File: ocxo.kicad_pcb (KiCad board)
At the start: 2 copper layers, 50 x 50 mm, 21 parts, among them J1 Conn_01x02, J2 Conn_01x01, J3 Conn_Coaxial, J4 Conn_01x01, J5 Conn_01x01, J6 Conn_01x01, J7 Conn_Coaxial, Q1 ENE3311 OCXO, U1 KA78M05_TO252, U2 LM4140

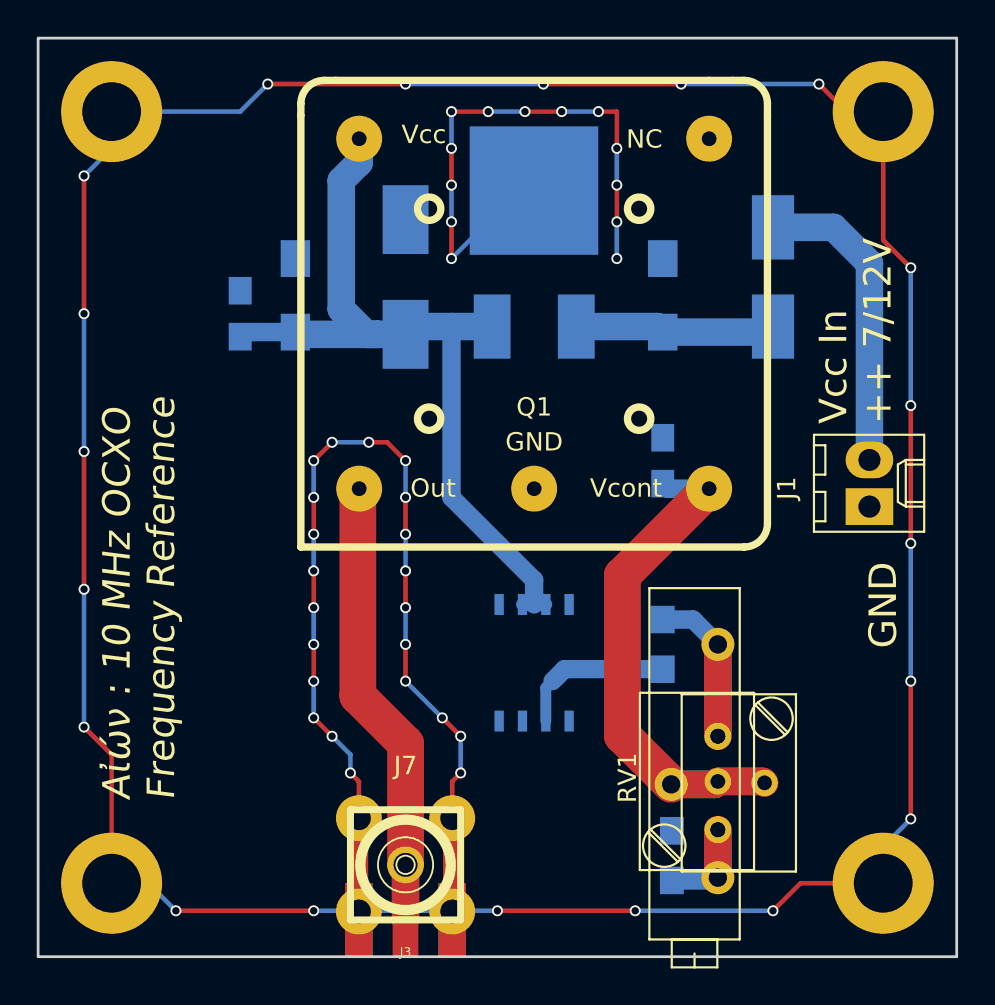
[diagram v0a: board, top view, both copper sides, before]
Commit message: via stitching added, new gerber
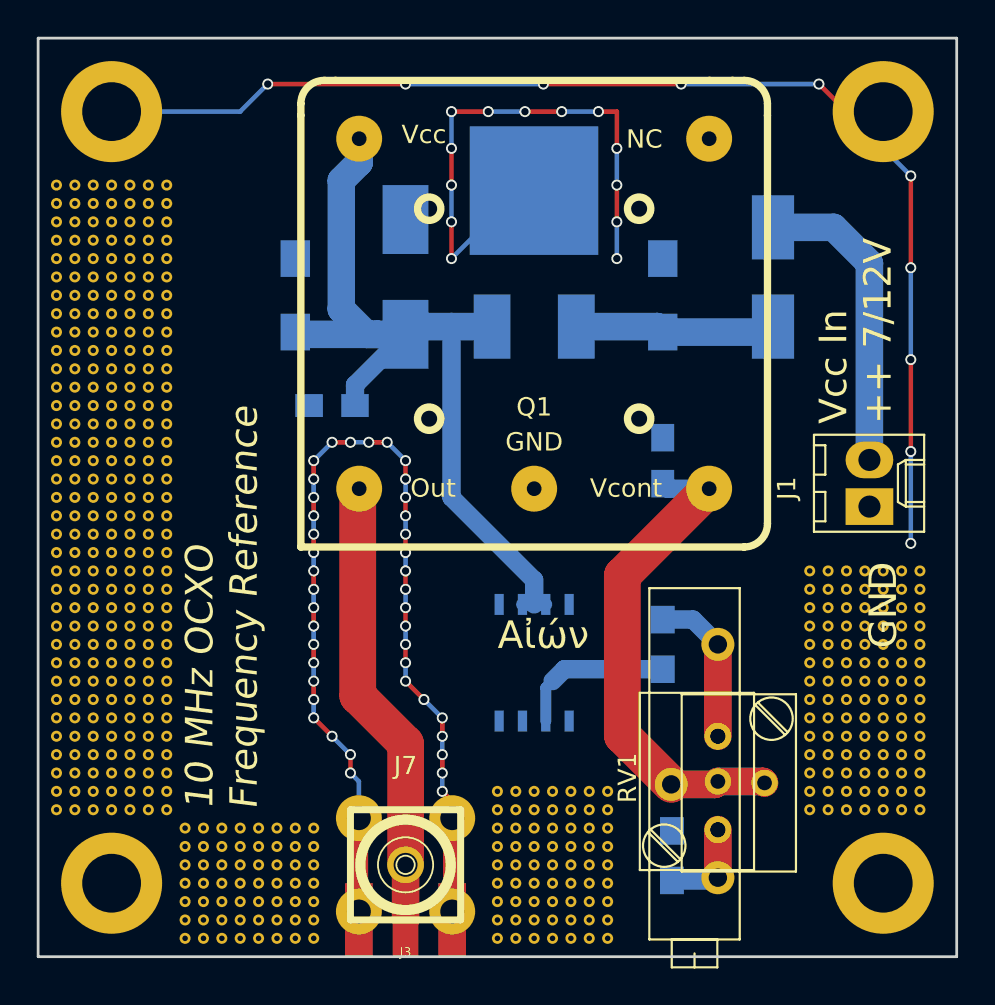
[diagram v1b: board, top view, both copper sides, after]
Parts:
- added REF**: via, via:via, F.Cu at (128.0, 87.0)
- added REF**: via, via:via, F.Cu at (126.0, 86.0)
- added REF**: via, via:via, F.Cu at (93.0, 94.0)
- added REF**: via, via:via, F.Cu at (92.0, 94.0)
- added REF**: via, via:via, F.Cu at (91.0, 94.0)
- added REF**: via, via:via, F.Cu at (90.0, 94.0)
- added REF**: via, via:via, F.Cu at (89.0, 94.0)
- added REF**: via, via:via, F.Cu at (88.0, 94.0)
- added REF**: via, via:via, F.Cu at (95.0, 93.0)
- added REF**: via, via:via, F.Cu at (94.0, 93.0)
- added REF**: via, via:via, F.Cu at (93.0, 93.0)
- added REF**: via, via:via, F.Cu at (92.0, 93.0)
- added REF**: via, via:via, F.Cu at (125.0, 86.0)
- added REF**: via, via:via, F.Cu at (91.0, 93.0)
- added REF**: via, via:via, F.Cu at (90.0, 93.0)
- added REF**: via, via:via, F.Cu at (89.0, 93.0)
- added REF**: via, via:via, F.Cu at (88.0, 93.0)
- added REF**: via, via:via, F.Cu at (95.0, 92.0)
- added REF**: via, via:via, F.Cu at (94.0, 92.0)
- added REF**: via, via:via, F.Cu at (93.0, 92.0)
- added REF**: via, via:via, F.Cu at (92.0, 92.0)
- added REF**: via, via:via, F.Cu at (91.0, 92.0)
- added REF**: via, via:via, F.Cu at (90.0, 92.0)
- added REF**: via, via:via, F.Cu at (124.0, 86.0)
- added REF**: via, via:via, F.Cu at (89.0, 92.0)
- added REF**: via, via:via, F.Cu at (88.0, 92.0)
- added REF**: via, via:via, F.Cu at (95.0, 91.0)
- added REF**: via, via:via, F.Cu at (94.0, 91.0)
- added REF**: via, via:via, F.Cu at (93.0, 91.0)
- added REF**: via, via:via, F.Cu at (92.0, 91.0)
- added REF**: via, via:via, F.Cu at (91.0, 91.0)
- added REF**: via, via:via, F.Cu at (90.0, 91.0)
- added REF**: via, via:via, F.Cu at (89.0, 91.0)
- added REF**: via, via:via, F.Cu at (88.0, 91.0)
- added REF**: via, via:via, F.Cu at (123.0, 86.0)
- added REF**: via, via:via, F.Cu at (95.0, 90.0)
- added REF**: via, via:via, F.Cu at (94.0, 90.0)
- added REF**: via, via:via, F.Cu at (93.0, 90.0)
- added REF**: via, via:via, F.Cu at (92.0, 90.0)
- added REF**: via, via:via, F.Cu at (91.0, 90.0)
- added REF**: via, via:via, F.Cu at (90.0, 90.0)
- added REF**: via, via:via, F.Cu at (89.0, 90.0)
- added REF**: via, via:via, F.Cu at (88.0, 90.0)
- added REF**: via, via:via, F.Cu at (95.0, 89.0)
- added REF**: via, via:via, F.Cu at (94.0, 89.0)
- added REF**: via, via:via, F.Cu at (122.0, 86.0)
- added REF**: via, via:via, F.Cu at (93.0, 89.0)
- added REF**: via, via:via, F.Cu at (92.0, 89.0)
- added REF**: via, via:via, F.Cu at (91.0, 89.0)
- added REF**: via, via:via, F.Cu at (90.0, 89.0)
- added REF**: via, via:via, F.Cu at (89.0, 89.0)
- added REF**: via, via:via, F.Cu at (88.0, 89.0)
- added REF**: via, via:via, F.Cu at (95.0, 88.0)
- added REF**: via, via:via, F.Cu at (94.0, 88.0)
- added REF**: via, via:via, F.Cu at (93.0, 88.0)
- added REF**: via, via:via, F.Cu at (92.0, 88.0)
- added REF**: via, via:via, F.Cu at (128.0, 85.0)
- added REF**: via, via:via, F.Cu at (91.0, 88.0)
- added REF**: via, via:via, F.Cu at (90.0, 88.0)
- added REF**: via, via:via, F.Cu at (89.0, 88.0)
- added REF**: via, via:via, F.Cu at (111.0, 94.0)
- added REF**: via, via:via, F.Cu at (110.0, 94.0)
- added REF**: via, via:via, F.Cu at (109.0, 94.0)
- added REF**: via, via:via, F.Cu at (108.0, 94.0)
- added REF**: via, via:via, F.Cu at (107.0, 94.0)
- added REF**: via, via:via, F.Cu at (106.0, 94.0)
- added REF**: via, via:via, F.Cu at (105.0, 94.0)
- added REF**: via, via:via, F.Cu at (127.0, 85.0)
- added REF**: via, via:via, F.Cu at (111.0, 93.0)
- added REF**: via, via:via, F.Cu at (110.0, 93.0)
- added REF**: via, via:via, F.Cu at (109.0, 93.0)
- added REF**: via, via:via, F.Cu at (108.0, 93.0)
- added REF**: via, via:via, F.Cu at (107.0, 93.0)
- added REF**: via, via:via, F.Cu at (106.0, 93.0)
- added REF**: via, via:via, F.Cu at (105.0, 93.0)
- added REF**: via, via:via, F.Cu at (111.0, 92.0)
- added REF**: via, via:via, F.Cu at (110.0, 92.0)
- added REF**: via, via:via, F.Cu at (109.0, 92.0)
- added REF**: via, via:via, F.Cu at (126.0, 85.0)
- added REF**: via, via:via, F.Cu at (108.0, 92.0)
- added REF**: via, via:via, F.Cu at (107.0, 92.0)
- added REF**: via, via:via, F.Cu at (106.0, 92.0)
- added REF**: via, via:via, F.Cu at (105.0, 92.0)
- added REF**: via, via:via, F.Cu at (111.0, 91.0)
- added REF**: via, via:via, F.Cu at (110.0, 91.0)
- added REF**: via, via:via, F.Cu at (109.0, 91.0)
- added REF**: via, via:via, F.Cu at (108.0, 91.0)
- added REF**: via, via:via, F.Cu at (107.0, 91.0)
- added REF**: via, via:via, F.Cu at (106.0, 91.0)
- added REF**: via, via:via, F.Cu at (125.0, 85.0)
- added REF**: via, via:via, F.Cu at (105.0, 91.0)
- added REF**: via, via:via, F.Cu at (111.0, 90.0)
- added REF**: via, via:via, F.Cu at (110.0, 90.0)
- added REF**: via, via:via, F.Cu at (109.0, 90.0)
- added REF**: via, via:via, F.Cu at (108.0, 90.0)
- added REF**: via, via:via, F.Cu at (107.0, 90.0)
- added REF**: via, via:via, F.Cu at (106.0, 90.0)
- added REF**: via, via:via, F.Cu at (105.0, 90.0)
- added REF**: via, via:via, F.Cu at (111.0, 89.0)
- added REF**: via, via:via, F.Cu at (110.0, 89.0)
- added REF**: via, via:via, F.Cu at (124.0, 85.0)
- added REF**: via, via:via, F.Cu at (109.0, 89.0)
- added REF**: via, via:via, F.Cu at (108.0, 89.0)
- added REF**: via, via:via, F.Cu at (107.0, 89.0)
- added REF**: via, via:via, F.Cu at (106.0, 89.0)
- added REF**: via, via:via, F.Cu at (105.0, 89.0)
- added REF**: via, via:via, F.Cu at (111.0, 88.0)
- added REF**: via, via:via, F.Cu at (110.0, 88.0)
- added REF**: via, via:via, F.Cu at (109.0, 88.0)
- added REF**: via, via:via, F.Cu at (108.0, 88.0)
- added REF**: via, via:via, F.Cu at (107.0, 88.0)
- added REF**: via, via:via, F.Cu at (127.0, 87.0)
- added REF**: via, via:via, F.Cu at (123.0, 85.0)
- added REF**: via, via:via, F.Cu at (106.0, 88.0)
- added REF**: via, via:via, F.Cu at (105.0, 88.0)
- added REF**: via, via:via, F.Cu at (111.0, 87.0)
- added REF**: via, via:via, F.Cu at (110.0, 87.0)
- added REF**: via, via:via, F.Cu at (109.0, 87.0)
- added REF**: via, via:via, F.Cu at (108.0, 87.0)
- added REF**: via, via:via, F.Cu at (107.0, 87.0)
- added REF**: via, via:via, F.Cu at (106.0, 87.0)
- added REF**: via, via:via, F.Cu at (105.0, 87.0)
- added REF**: via, via:via, F.Cu at (111.0, 86.0)
- added REF**: via, via:via, F.Cu at (122.0, 85.0)
- added REF**: via, via:via, F.Cu at (110.0, 86.0)
- added REF**: via, via:via, F.Cu at (109.0, 86.0)
- added REF**: via, via:via, F.Cu at (108.0, 86.0)
- added REF**: via, via:via, F.Cu at (107.0, 86.0)
- added REF**: via, via:via, F.Cu at (106.0, 86.0)
- added REF**: via, via:via, F.Cu at (87.0, 87.0)
- added REF**: via, via:via, F.Cu at (86.0, 87.0)
- added REF**: via, via:via, F.Cu at (85.0, 87.0)
- added REF**: via, via:via, F.Cu at (84.0, 87.0)
- added REF**: via, via:via, F.Cu at (83.0, 87.0)
- added REF**: via, via:via, F.Cu at (128.0, 84.0)
- added REF**: via, via:via, F.Cu at (82.0, 87.0)
- added REF**: via, via:via, F.Cu at (81.0, 87.0)
- added REF**: via, via:via, F.Cu at (87.0, 86.0)
- added REF**: via, via:via, F.Cu at (86.0, 86.0)
- added REF**: via, via:via, F.Cu at (85.0, 86.0)
- added REF**: via, via:via, F.Cu at (84.0, 86.0)
- added REF**: via, via:via, F.Cu at (83.0, 86.0)
- added REF**: via, via:via, F.Cu at (82.0, 86.0)
- added REF**: via, via:via, F.Cu at (81.0, 86.0)
- added REF**: via, via:via, F.Cu at (87.0, 85.0)
- added REF**: via, via:via, F.Cu at (127.0, 84.0)
- added REF**: via, via:via, F.Cu at (86.0, 85.0)
- added REF**: via, via:via, F.Cu at (85.0, 85.0)
- added REF**: via, via:via, F.Cu at (84.0, 85.0)
- added REF**: via, via:via, F.Cu at (83.0, 85.0)
- added REF**: via, via:via, F.Cu at (82.0, 85.0)
- added REF**: via, via:via, F.Cu at (81.0, 85.0)
- added REF**: via, via:via, F.Cu at (87.0, 84.0)
- added REF**: via, via:via, F.Cu at (86.0, 84.0)
- added REF**: via, via:via, F.Cu at (85.0, 84.0)
- added REF**: via, via:via, F.Cu at (84.0, 84.0)
- added REF**: via, via:via, F.Cu at (126.0, 84.0)
- added REF**: via, via:via, F.Cu at (83.0, 84.0)
- added REF**: via, via:via, F.Cu at (82.0, 84.0)
- added REF**: via, via:via, F.Cu at (81.0, 84.0)
- added REF**: via, via:via, F.Cu at (87.0, 83.0)
- added REF**: via, via:via, F.Cu at (86.0, 83.0)
- added REF**: via, via:via, F.Cu at (85.0, 83.0)
- added REF**: via, via:via, F.Cu at (84.0, 83.0)
- added REF**: via, via:via, F.Cu at (83.0, 83.0)
- added REF**: via, via:via, F.Cu at (82.0, 83.0)
- added REF**: via, via:via, F.Cu at (81.0, 83.0)
- added REF**: via, via:via, F.Cu at (125.0, 84.0)
- added REF**: via, via:via, F.Cu at (87.0, 82.0)
- added REF**: via, via:via, F.Cu at (86.0, 82.0)
- added REF**: via, via:via, F.Cu at (85.0, 82.0)
- added REF**: via, via:via, F.Cu at (84.0, 82.0)
- added REF**: via, via:via, F.Cu at (83.0, 82.0)
- added REF**: via, via:via, F.Cu at (82.0, 82.0)
- added REF**: via, via:via, F.Cu at (81.0, 82.0)
- added REF**: via, via:via, F.Cu at (87.0, 81.0)
- added REF**: via, via:via, F.Cu at (86.0, 81.0)
- added REF**: via, via:via, F.Cu at (85.0, 81.0)
- added REF**: via, via:via, F.Cu at (124.0, 84.0)
- added REF**: via, via:via, F.Cu at (84.0, 81.0)
- added REF**: via, via:via, F.Cu at (83.0, 81.0)
- added REF**: via, via:via, F.Cu at (82.0, 81.0)
- added REF**: via, via:via, F.Cu at (81.0, 81.0)
- added REF**: via, via:via, F.Cu at (87.0, 80.0)
- added REF**: via, via:via, F.Cu at (86.0, 80.0)
- added REF**: via, via:via, F.Cu at (85.0, 80.0)
- added REF**: via, via:via, F.Cu at (84.0, 80.0)
- added REF**: via, via:via, F.Cu at (83.0, 80.0)
- added REF**: via, via:via, F.Cu at (82.0, 80.0)
- added REF**: via, via:via, F.Cu at (123.0, 84.0)
- added REF**: via, via:via, F.Cu at (81.0, 80.0)
- added REF**: via, via:via, F.Cu at (87.0, 79.0)
- added REF**: via, via:via, F.Cu at (86.0, 79.0)
- added REF**: via, via:via, F.Cu at (85.0, 79.0)
- added REF**: via, via:via, F.Cu at (84.0, 79.0)
- added REF**: via, via:via, F.Cu at (83.0, 79.0)
- added REF**: via, via:via, F.Cu at (82.0, 79.0)
- added REF**: via, via:via, F.Cu at (81.0, 79.0)
- added REF**: via, via:via, F.Cu at (87.0, 78.0)
- added REF**: via, via:via, F.Cu at (86.0, 78.0)
- added REF**: via, via:via, F.Cu at (122.0, 84.0)
- added REF**: via, via:via, F.Cu at (85.0, 78.0)
- added REF**: via, via:via, F.Cu at (84.0, 78.0)
- added REF**: via, via:via, F.Cu at (83.0, 78.0)
- added REF**: via, via:via, F.Cu at (82.0, 78.0)
- added REF**: via, via:via, F.Cu at (81.0, 78.0)
- added REF**: via, via:via, F.Cu at (87.0, 77.0)
- added REF**: via, via:via, F.Cu at (86.0, 77.0)
- added REF**: via, via:via, F.Cu at (85.0, 77.0)
- added REF**: via, via:via, F.Cu at (84.0, 77.0)
- added REF**: via, via:via, F.Cu at (83.0, 77.0)
- added REF**: via, via:via, F.Cu at (128.0, 83.0)
- added REF**: via, via:via, F.Cu at (82.0, 77.0)
- added REF**: via, via:via, F.Cu at (81.0, 77.0)
- added REF**: via, via:via, F.Cu at (87.0, 76.0)
- added REF**: via, via:via, F.Cu at (86.0, 76.0)
- added REF**: via, via:via, F.Cu at (85.0, 76.0)
- added REF**: via, via:via, F.Cu at (84.0, 76.0)
- added REF**: via, via:via, F.Cu at (83.0, 76.0)
- added REF**: via, via:via, F.Cu at (82.0, 76.0)
- added REF**: via, via:via, F.Cu at (81.0, 76.0)
- added REF**: via, via:via, F.Cu at (87.0, 75.0)
- added REF**: via, via:via, F.Cu at (126.0, 87.0)
- added REF**: via, via:via, F.Cu at (127.0, 83.0)
- added REF**: via, via:via, F.Cu at (86.0, 75.0)
- added REF**: via, via:via, F.Cu at (85.0, 75.0)
- added REF**: via, via:via, F.Cu at (84.0, 75.0)
- added REF**: via, via:via, F.Cu at (83.0, 75.0)
- added REF**: via, via:via, F.Cu at (82.0, 75.0)
- added REF**: via, via:via, F.Cu at (81.0, 75.0)
- added REF**: via, via:via, F.Cu at (87.0, 74.0)
- added REF**: via, via:via, F.Cu at (86.0, 74.0)
- added REF**: via, via:via, F.Cu at (85.0, 74.0)
- added REF**: via, via:via, F.Cu at (84.0, 74.0)
- added REF**: via, via:via, F.Cu at (126.0, 83.0)
- added REF**: via, via:via, F.Cu at (83.0, 74.0)
- added REF**: via, via:via, F.Cu at (82.0, 74.0)
- added REF**: via, via:via, F.Cu at (81.0, 74.0)
- added REF**: via, via:via, F.Cu at (87.0, 73.0)
- added REF**: via, via:via, F.Cu at (86.0, 73.0)
- added REF**: via, via:via, F.Cu at (85.0, 73.0)
- added REF**: via, via:via, F.Cu at (84.0, 73.0)
- added REF**: via, via:via, F.Cu at (83.0, 73.0)
- added REF**: via, via:via, F.Cu at (82.0, 73.0)
- added REF**: via, via:via, F.Cu at (81.0, 73.0)
- added REF**: via, via:via, F.Cu at (125.0, 83.0)
- added REF**: via, via:via, F.Cu at (87.0, 72.0)
- added REF**: via, via:via, F.Cu at (86.0, 72.0)
- added REF**: via, via:via, F.Cu at (85.0, 72.0)
- added REF**: via, via:via, F.Cu at (84.0, 72.0)
- added REF**: via, via:via, F.Cu at (83.0, 72.0)
- added REF**: via, via:via, F.Cu at (82.0, 72.0)
- added REF**: via, via:via, F.Cu at (81.0, 72.0)
- added REF**: via, via:via, F.Cu at (87.0, 71.0)
- added REF**: via, via:via, F.Cu at (86.0, 71.0)
- added REF**: via, via:via, F.Cu at (85.0, 71.0)
- added REF**: via, via:via, F.Cu at (124.0, 83.0)
- added REF**: via, via:via, F.Cu at (84.0, 71.0)
- added REF**: via, via:via, F.Cu at (83.0, 71.0)
- added REF**: via, via:via, F.Cu at (82.0, 71.0)
- added REF**: via, via:via, F.Cu at (81.0, 71.0)
- added REF**: via, via:via, F.Cu at (87.0, 70.0)
- added REF**: via, via:via, F.Cu at (86.0, 70.0)
- added REF**: via, via:via, F.Cu at (85.0, 70.0)
- added REF**: via, via:via, F.Cu at (84.0, 70.0)
- added REF**: via, via:via, F.Cu at (83.0, 70.0)
- added REF**: via, via:via, F.Cu at (82.0, 70.0)
- added REF**: via, via:via, F.Cu at (123.0, 83.0)
- added REF**: via, via:via, F.Cu at (81.0, 70.0)
- added REF**: via, via:via, F.Cu at (87.0, 69.0)
- added REF**: via, via:via, F.Cu at (86.0, 69.0)
- added REF**: via, via:via, F.Cu at (85.0, 69.0)
- added REF**: via, via:via, F.Cu at (84.0, 69.0)
- added REF**: via, via:via, F.Cu at (83.0, 69.0)
- added REF**: via, via:via, F.Cu at (82.0, 69.0)
- added REF**: via, via:via, F.Cu at (81.0, 69.0)
- added REF**: via, via:via, F.Cu at (87.0, 68.0)
- added REF**: via, via:via, F.Cu at (86.0, 68.0)
- added REF**: via, via:via, F.Cu at (122.0, 83.0)
- added REF**: via, via:via, F.Cu at (85.0, 68.0)
- added REF**: via, via:via, F.Cu at (84.0, 68.0)
- added REF**: via, via:via, F.Cu at (83.0, 68.0)
- added REF**: via, via:via, F.Cu at (82.0, 68.0)
- added REF**: via, via:via, F.Cu at (81.0, 68.0)
- added REF**: via, via:via, F.Cu at (87.0, 67.0)
- added REF**: via, via:via, F.Cu at (86.0, 67.0)
- added REF**: via, via:via, F.Cu at (85.0, 67.0)
- added REF**: via, via:via, F.Cu at (84.0, 67.0)
- added REF**: via, via:via, F.Cu at (83.0, 67.0)
- added REF**: via, via:via, F.Cu at (128.0, 82.0)
- added REF**: via, via:via, F.Cu at (82.0, 67.0)
- added REF**: via, via:via, F.Cu at (81.0, 67.0)
- added REF**: via, via:via, F.Cu at (87.0, 66.0)
- added REF**: via, via:via, F.Cu at (86.0, 66.0)
- added REF**: via, via:via, F.Cu at (85.0, 66.0)
- added REF**: via, via:via, F.Cu at (84.0, 66.0)
- added REF**: via, via:via, F.Cu at (83.0, 66.0)
- added REF**: via, via:via, F.Cu at (82.0, 66.0)
- added REF**: via, via:via, F.Cu at (81.0, 66.0)
- added REF**: via, via:via, F.Cu at (87.0, 65.0)
- added REF**: via, via:via, F.Cu at (127.0, 82.0)
- added REF**: via, via:via, F.Cu at (86.0, 65.0)
- added REF**: via, via:via, F.Cu at (85.0, 65.0)
- added REF**: via, via:via, F.Cu at (84.0, 65.0)
- added REF**: via, via:via, F.Cu at (83.0, 65.0)
- added REF**: via, via:via, F.Cu at (82.0, 65.0)
- added REF**: via, via:via, F.Cu at (81.0, 65.0)
- added REF**: via, via:via, F.Cu at (87.0, 64.0)
- added REF**: via, via:via, F.Cu at (86.0, 64.0)
- added REF**: via, via:via, F.Cu at (85.0, 64.0)
- added REF**: via, via:via, F.Cu at (84.0, 64.0)
- added REF**: via, via:via, F.Cu at (126.0, 82.0)
- added REF**: via, via:via, F.Cu at (83.0, 64.0)
- added REF**: via, via:via, F.Cu at (82.0, 64.0)
- added REF**: via, via:via, F.Cu at (81.0, 64.0)
- added REF**: via, via:via, F.Cu at (87.0, 63.0)
- added REF**: via, via:via, F.Cu at (86.0, 63.0)
- added REF**: via, via:via, F.Cu at (85.0, 63.0)
- added REF**: via, via:via, F.Cu at (84.0, 63.0)
- added REF**: via, via:via, F.Cu at (83.0, 63.0)
- added REF**: via, via:via, F.Cu at (82.0, 63.0)
- added REF**: via, via:via, F.Cu at (81.0, 63.0)
- added REF**: via, via:via, F.Cu at (125.0, 82.0)
- added REF**: via, via:via, F.Cu at (87.0, 62.0)
- added REF**: via, via:via, F.Cu at (86.0, 62.0)
- added REF**: via, via:via, F.Cu at (85.0, 62.0)
- added REF**: via, via:via, F.Cu at (84.0, 62.0)
- added REF**: via, via:via, F.Cu at (83.0, 62.0)
- added REF**: via, via:via, F.Cu at (82.0, 62.0)
- added REF**: via, via:via, F.Cu at (81.0, 62.0)
- added REF**: via, via:via, F.Cu at (87.0, 61.0)
- added REF**: via, via:via, F.Cu at (86.0, 61.0)
- added REF**: via, via:via, F.Cu at (85.0, 61.0)
- added REF**: via, via:via, F.Cu at (125.0, 87.0)
- added REF**: via, via:via, F.Cu at (124.0, 82.0)
- added REF**: via, via:via, F.Cu at (84.0, 61.0)
- added REF**: via, via:via, F.Cu at (83.0, 61.0)
- added REF**: via, via:via, F.Cu at (82.0, 61.0)
- added REF**: via, via:via, F.Cu at (81.0, 61.0)
- added REF**: via, via:via, F.Cu at (87.0, 60.0)
- added REF**: via, via:via, F.Cu at (86.0, 60.0)
- added REF**: via, via:via, F.Cu at (85.0, 60.0)
- added REF**: via, via:via, F.Cu at (84.0, 60.0)
- added REF**: via, via:via, F.Cu at (83.0, 60.0)
- added REF**: via, via:via, F.Cu at (82.0, 60.0)
- added REF**: via, via:via, F.Cu at (123.0, 82.0)
- added REF**: via, via:via, F.Cu at (81.0, 60.0)
- added REF**: via, via:via, F.Cu at (87.0, 59.0)
- added REF**: via, via:via, F.Cu at (86.0, 59.0)
- added REF**: via, via:via, F.Cu at (85.0, 59.0)
- added REF**: via, via:via, F.Cu at (84.0, 59.0)
- added REF**: via, via:via, F.Cu at (83.0, 59.0)
- added REF**: via, via:via, F.Cu at (82.0, 59.0)
- added REF**: via, via:via, F.Cu at (81.0, 59.0)
- added REF**: via, via:via, F.Cu at (87.0, 58.0)
- added REF**: via, via:via, F.Cu at (86.0, 58.0)
- added REF**: via, via:via, F.Cu at (122.0, 82.0)
- added REF**: via, via:via, F.Cu at (85.0, 58.0)
- added REF**: via, via:via, F.Cu at (84.0, 58.0)
- added REF**: via, via:via, F.Cu at (83.0, 58.0)
- added REF**: via, via:via, F.Cu at (82.0, 58.0)
- added REF**: via, via:via, F.Cu at (81.0, 58.0)
- added REF**: via, via:via, F.Cu at (87.0, 57.0)
- added REF**: via, via:via, F.Cu at (86.0, 57.0)
- added REF**: via, via:via, F.Cu at (85.0, 57.0)
- added REF**: via, via:via, F.Cu at (84.0, 57.0)
- added REF**: via, via:via, F.Cu at (83.0, 57.0)
- added REF**: via, via:via, F.Cu at (128.0, 81.0)
- added REF**: via, via:via, F.Cu at (82.0, 57.0)
- added REF**: via, via:via, F.Cu at (81.0, 57.0)
- added REF**: via, via:via, F.Cu at (87.0, 56.0)
- added REF**: via, via:via, F.Cu at (86.0, 56.0)
- added REF**: via, via:via, F.Cu at (85.0, 56.0)
- added REF**: via, via:via, F.Cu at (84.0, 56.0)
- added REF**: via, via:via, F.Cu at (83.0, 56.0)
- added REF**: via, via:via, F.Cu at (82.0, 56.0)
- added REF**: via, via:via, F.Cu at (81.0, 56.0)
- added REF**: via, via:via, F.Cu at (87.0, 55.0)
- added REF**: via, via:via, F.Cu at (127.0, 81.0)
- added REF**: via, via:via, F.Cu at (86.0, 55.0)
- added REF**: via, via:via, F.Cu at (85.0, 55.0)
- added REF**: via, via:via, F.Cu at (84.0, 55.0)
- added REF**: via, via:via, F.Cu at (83.0, 55.0)
- added REF**: via, via:via, F.Cu at (82.0, 55.0)
- added REF**: via, via:via, F.Cu at (81.0, 55.0)
- added REF**: via, via:via, F.Cu at (87.0, 54.0)
- added REF**: via, via:via, F.Cu at (86.0, 54.0)
- added REF**: via, via:via, F.Cu at (85.0, 54.0)
- added REF**: via, via:via, F.Cu at (84.0, 54.0)
- added REF**: via, via:via, F.Cu at (126.0, 81.0)
- added REF**: via, via:via, F.Cu at (83.0, 54.0)
- added REF**: via, via:via, F.Cu at (82.0, 54.0)
- added REF**: via, via:via, F.Cu at (81.0, 54.0)
- added REF**: via, via:via, F.Cu at (87.0, 53.0)
- added REF**: via, via:via, F.Cu at (86.0, 53.0)
- added REF**: via, via:via, F.Cu at (85.0, 53.0)
- added REF**: via, via:via, F.Cu at (84.0, 53.0)
- added REF**: via, via:via, F.Cu at (83.0, 53.0)
- added REF**: via, via:via, F.Cu at (82.0, 53.0)
- added REF**: via, via:via, F.Cu at (81.0, 53.0)
- added REF**: via, via:via, F.Cu at (125.0, 81.0)
- added REF**: via, via:via, F.Cu at (105.0, 86.0)
- added REF**: via, via:via, F.Cu at (88.0, 88.0)
- added REF**: via, via:via, F.Cu at (122.0, 74.0)
- added REF**: via, via:via, F.Cu at (124.0, 81.0)
- added REF**: via, via:via, F.Cu at (123.0, 81.0)
- added REF**: via, via:via, F.Cu at (122.0, 81.0)
- added REF**: via, via:via, F.Cu at (124.0, 87.0)
- added REF**: via, via:via, F.Cu at (128.0, 80.0)
- added REF**: via, via:via, F.Cu at (127.0, 80.0)
- added REF**: via, via:via, F.Cu at (126.0, 80.0)
- added REF**: via, via:via, F.Cu at (125.0, 80.0)
- added REF**: via, via:via, F.Cu at (124.0, 80.0)
- added REF**: via, via:via, F.Cu at (123.0, 80.0)
- added REF**: via, via:via, F.Cu at (122.0, 80.0)
- added REF**: via, via:via, F.Cu at (128.0, 79.0)
- added REF**: via, via:via, F.Cu at (127.0, 79.0)
- added REF**: via, via:via, F.Cu at (126.0, 79.0)
- added REF**: via, via:via, F.Cu at (123.0, 87.0)
- added REF**: via, via:via, F.Cu at (125.0, 79.0)
- added REF**: via, via:via, F.Cu at (124.0, 79.0)
- added REF**: via, via:via, F.Cu at (123.0, 79.0)
- added REF**: via, via:via, F.Cu at (122.0, 79.0)
- added REF**: via, via:via, F.Cu at (128.0, 78.0)
- added REF**: via, via:via, F.Cu at (127.0, 78.0)
- added REF**: via, via:via, F.Cu at (126.0, 78.0)
- added REF**: via, via:via, F.Cu at (125.0, 78.0)
- added REF**: via, via:via, F.Cu at (124.0, 78.0)
- added REF**: via, via:via, F.Cu at (123.0, 78.0)
- added REF**: via, via:via, F.Cu at (122.0, 87.0)
- added REF**: via, via:via, F.Cu at (122.0, 78.0)
- added REF**: via, via:via, F.Cu at (128.0, 77.0)
- added REF**: via, via:via, F.Cu at (127.0, 77.0)
- added REF**: via, via:via, F.Cu at (126.0, 77.0)
- added REF**: via, via:via, F.Cu at (125.0, 77.0)
- added REF**: via, via:via, F.Cu at (124.0, 77.0)
- added REF**: via, via:via, F.Cu at (123.0, 77.0)
- added REF**: via, via:via, F.Cu at (122.0, 77.0)
- added REF**: via, via:via, F.Cu at (128.0, 76.0)
- added REF**: via, via:via, F.Cu at (127.0, 76.0)
- added REF**: via, via:via, F.Cu at (128.0, 86.0)
- added REF**: via, via:via, F.Cu at (126.0, 76.0)
- added REF**: via, via:via, F.Cu at (125.0, 76.0)
- added REF**: via, via:via, F.Cu at (124.0, 76.0)
- added REF**: via, via:via, F.Cu at (123.0, 76.0)
- added REF**: via, via:via, F.Cu at (122.0, 76.0)
- added REF**: via, via:via, F.Cu at (128.0, 75.0)
- added REF**: via, via:via, F.Cu at (127.0, 75.0)
- added REF**: via, via:via, F.Cu at (126.0, 75.0)
- added REF**: via, via:via, F.Cu at (125.0, 75.0)
- added REF**: via, via:via, F.Cu at (124.0, 75.0)
- added REF**: via, via:via, F.Cu at (127.0, 86.0)
- added REF**: via, via:via, F.Cu at (123.0, 75.0)
- added REF**: via, via:via, F.Cu at (122.0, 75.0)
- added REF**: via, via:via, F.Cu at (128.0, 74.0)
- added REF**: via, via:via, F.Cu at (127.0, 74.0)
- added REF**: via, via:via, F.Cu at (126.0, 74.0)
- added REF**: via, via:via, F.Cu at (125.0, 74.0)
- added REF**: via, via:via, F.Cu at (124.0, 74.0)
- added REF**: via, via:via, F.Cu at (123.0, 74.0)
- added REF**: via, via:via, F.Cu at (95.0, 94.0)
- added REF**: via, via:via, F.Cu at (94.0, 94.0)
- moved C2 7.07 mm to (96.0, 65.0), turned to 180 degrees
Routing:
- net GND: track 271.5 -> 171.6 mm, vias 56 -> 65
- net Net-(C2-Pad1): track 44.5 -> 46.5 mm
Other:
- board text added: "10 MHz OCXO Frequency Reference"
- board text added: "Αἰών"
- board text removed: "Αἰών : 10 MHz OCXO Frequency Reference"

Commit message: via stitching added, new gerber
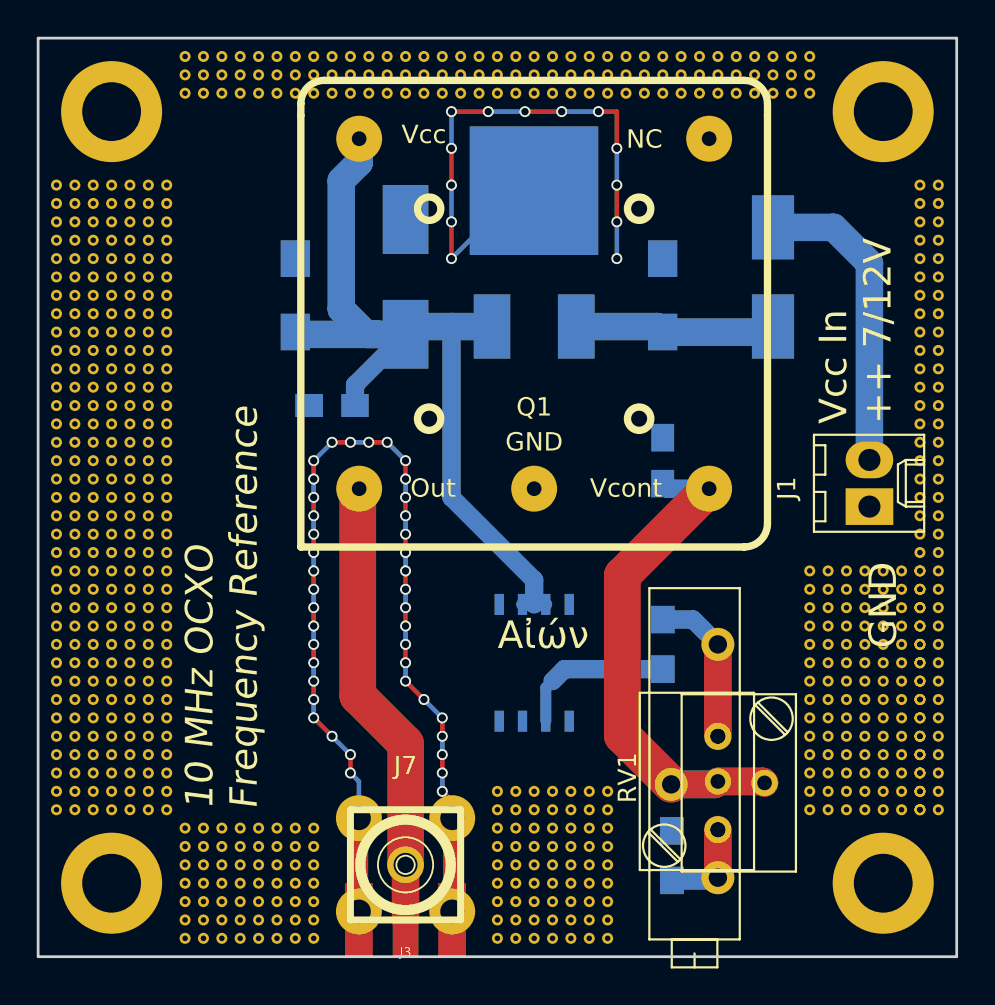
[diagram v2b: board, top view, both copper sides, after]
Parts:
- added REF**: via, via:via, F.Cu at (129.0, 87.0)
- added REF**: via, via:via, F.Cu at (128.0, 83.0)
- added REF**: via, via:via, F.Cu at (93.0, 48.0)
- added REF**: via, via:via, F.Cu at (92.0, 48.0)
- added REF**: via, via:via, F.Cu at (91.0, 48.0)
- added REF**: via, via:via, F.Cu at (90.0, 48.0)
- added REF**: via, via:via, F.Cu at (89.0, 48.0)
- added REF**: via, via:via, F.Cu at (88.0, 48.0)
- added REF**: via, via:via, F.Cu at (122.0, 47.0)
- added REF**: via, via:via, F.Cu at (121.0, 47.0)
- added REF**: via, via:via, F.Cu at (120.0, 47.0)
- added REF**: via, via:via, F.Cu at (119.0, 47.0)
- added REF**: via, via:via, F.Cu at (129.0, 82.0)
- added REF**: via, via:via, F.Cu at (118.0, 47.0)
- added REF**: via, via:via, F.Cu at (117.0, 47.0)
- added REF**: via, via:via, F.Cu at (116.0, 47.0)
- added REF**: via, via:via, F.Cu at (115.0, 47.0)
- added REF**: via, via:via, F.Cu at (114.0, 47.0)
- added REF**: via, via:via, F.Cu at (113.0, 47.0)
- added REF**: via, via:via, F.Cu at (112.0, 47.0)
- added REF**: via, via:via, F.Cu at (111.0, 47.0)
- added REF**: via, via:via, F.Cu at (110.0, 47.0)
- added REF**: via, via:via, F.Cu at (109.0, 47.0)
- added REF**: via, via:via, F.Cu at (128.0, 82.0)
- added REF**: via, via:via, F.Cu at (108.0, 47.0)
- added REF**: via, via:via, F.Cu at (107.0, 47.0)
- added REF**: via, via:via, F.Cu at (106.0, 47.0)
- added REF**: via, via:via, F.Cu at (105.0, 47.0)
- added REF**: via, via:via, F.Cu at (104.0, 47.0)
- added REF**: via, via:via, F.Cu at (103.0, 47.0)
- added REF**: via, via:via, F.Cu at (102.0, 47.0)
- added REF**: via, via:via, F.Cu at (101.0, 47.0)
- added REF**: via, via:via, F.Cu at (100.0, 47.0)
- added REF**: via, via:via, F.Cu at (99.0, 47.0)
- added REF**: via, via:via, F.Cu at (129.0, 81.0)
- added REF**: via, via:via, F.Cu at (98.0, 47.0)
- added REF**: via, via:via, F.Cu at (97.0, 47.0)
- added REF**: via, via:via, F.Cu at (96.0, 47.0)
- added REF**: via, via:via, F.Cu at (95.0, 47.0)
- added REF**: via, via:via, F.Cu at (94.0, 47.0)
- added REF**: via, via:via, F.Cu at (93.0, 47.0)
- added REF**: via, via:via, F.Cu at (92.0, 47.0)
- added REF**: via, via:via, F.Cu at (91.0, 47.0)
- added REF**: via, via:via, F.Cu at (90.0, 47.0)
- added REF**: via, via:via, F.Cu at (89.0, 47.0)
- added REF**: via, via:via, F.Cu at (128.0, 81.0)
- added REF**: via, via:via, F.Cu at (88.0, 47.0)
- added REF**: via, via:via, F.Cu at (122.0, 46.0)
- added REF**: via, via:via, F.Cu at (121.0, 46.0)
- added REF**: via, via:via, F.Cu at (120.0, 46.0)
- added REF**: via, via:via, F.Cu at (119.0, 46.0)
- added REF**: via, via:via, F.Cu at (118.0, 46.0)
- added REF**: via, via:via, F.Cu at (117.0, 46.0)
- added REF**: via, via:via, F.Cu at (116.0, 46.0)
- added REF**: via, via:via, F.Cu at (115.0, 46.0)
- added REF**: via, via:via, F.Cu at (114.0, 46.0)
- added REF**: via, via:via, F.Cu at (129.0, 80.0)
- added REF**: via, via:via, F.Cu at (113.0, 46.0)
- added REF**: via, via:via, F.Cu at (112.0, 46.0)
- added REF**: via, via:via, F.Cu at (111.0, 46.0)
- added REF**: via, via:via, F.Cu at (110.0, 46.0)
- added REF**: via, via:via, F.Cu at (109.0, 46.0)
- added REF**: via, via:via, F.Cu at (108.0, 46.0)
- added REF**: via, via:via, F.Cu at (107.0, 46.0)
- added REF**: via, via:via, F.Cu at (106.0, 46.0)
- added REF**: via, via:via, F.Cu at (105.0, 46.0)
- added REF**: via, via:via, F.Cu at (104.0, 46.0)
- added REF**: via, via:via, F.Cu at (128.0, 80.0)
- added REF**: via, via:via, F.Cu at (103.0, 46.0)
- added REF**: via, via:via, F.Cu at (102.0, 46.0)
- added REF**: via, via:via, F.Cu at (101.0, 46.0)
- added REF**: via, via:via, F.Cu at (100.0, 46.0)
- added REF**: via, via:via, F.Cu at (99.0, 46.0)
- added REF**: via, via:via, F.Cu at (98.0, 46.0)
- added REF**: via, via:via, F.Cu at (97.0, 46.0)
- added REF**: via, via:via, F.Cu at (96.0, 46.0)
- added REF**: via, via:via, F.Cu at (95.0, 46.0)
- added REF**: via, via:via, F.Cu at (94.0, 46.0)
- added REF**: via, via:via, F.Cu at (129.0, 79.0)
- added REF**: via, via:via, F.Cu at (93.0, 46.0)
- added REF**: via, via:via, F.Cu at (92.0, 46.0)
- added REF**: via, via:via, F.Cu at (91.0, 46.0)
- added REF**: via, via:via, F.Cu at (90.0, 46.0)
- added REF**: via, via:via, F.Cu at (89.0, 46.0)
- added REF**: via, via:via, F.Cu at (88.0, 46.0)
- added REF**: via, via:via, F.Cu at (128.0, 79.0)
- added REF**: via, via:via, F.Cu at (129.0, 78.0)
- added REF**: via, via:via, F.Cu at (128.0, 87.0)
- added REF**: via, via:via, F.Cu at (128.0, 78.0)
- added REF**: via, via:via, F.Cu at (129.0, 77.0)
- added REF**: via, via:via, F.Cu at (128.0, 77.0)
- added REF**: via, via:via, F.Cu at (129.0, 76.0)
- added REF**: via, via:via, F.Cu at (128.0, 76.0)
- added REF**: via, via:via, F.Cu at (129.0, 75.0)
- added REF**: via, via:via, F.Cu at (128.0, 75.0)
- added REF**: via, via:via, F.Cu at (129.0, 74.0)
- added REF**: via, via:via, F.Cu at (128.0, 74.0)
- added REF**: via, via:via, F.Cu at (129.0, 73.0)
- added REF**: via, via:via, F.Cu at (129.0, 86.0)
- added REF**: via, via:via, F.Cu at (128.0, 73.0)
- added REF**: via, via:via, F.Cu at (129.0, 72.0)
- added REF**: via, via:via, F.Cu at (128.0, 72.0)
- added REF**: via, via:via, F.Cu at (129.0, 71.0)
- added REF**: via, via:via, F.Cu at (128.0, 71.0)
- added REF**: via, via:via, F.Cu at (129.0, 70.0)
- added REF**: via, via:via, F.Cu at (128.0, 70.0)
- added REF**: via, via:via, F.Cu at (129.0, 69.0)
- added REF**: via, via:via, F.Cu at (128.0, 69.0)
- added REF**: via, via:via, F.Cu at (129.0, 68.0)
- added REF**: via, via:via, F.Cu at (128.0, 86.0)
- added REF**: via, via:via, F.Cu at (128.0, 68.0)
- added REF**: via, via:via, F.Cu at (129.0, 67.0)
- added REF**: via, via:via, F.Cu at (128.0, 67.0)
- added REF**: via, via:via, F.Cu at (129.0, 66.0)
- added REF**: via, via:via, F.Cu at (128.0, 66.0)
- added REF**: via, via:via, F.Cu at (129.0, 65.0)
- added REF**: via, via:via, F.Cu at (128.0, 65.0)
- added REF**: via, via:via, F.Cu at (129.0, 64.0)
- added REF**: via, via:via, F.Cu at (128.0, 64.0)
- added REF**: via, via:via, F.Cu at (129.0, 63.0)
- added REF**: via, via:via, F.Cu at (129.0, 85.0)
- added REF**: via, via:via, F.Cu at (128.0, 63.0)
- added REF**: via, via:via, F.Cu at (129.0, 62.0)
- added REF**: via, via:via, F.Cu at (128.0, 62.0)
- added REF**: via, via:via, F.Cu at (129.0, 61.0)
- added REF**: via, via:via, F.Cu at (128.0, 61.0)
- added REF**: via, via:via, F.Cu at (129.0, 60.0)
- added REF**: via, via:via, F.Cu at (128.0, 60.0)
- added REF**: via, via:via, F.Cu at (129.0, 59.0)
- added REF**: via, via:via, F.Cu at (128.0, 59.0)
- added REF**: via, via:via, F.Cu at (129.0, 58.0)
- added REF**: via, via:via, F.Cu at (128.0, 85.0)
- added REF**: via, via:via, F.Cu at (128.0, 58.0)
- added REF**: via, via:via, F.Cu at (129.0, 57.0)
- added REF**: via, via:via, F.Cu at (128.0, 57.0)
- added REF**: via, via:via, F.Cu at (129.0, 56.0)
- added REF**: via, via:via, F.Cu at (128.0, 56.0)
- added REF**: via, via:via, F.Cu at (129.0, 55.0)
- added REF**: via, via:via, F.Cu at (128.0, 55.0)
- added REF**: via, via:via, F.Cu at (129.0, 54.0)
- added REF**: via, via:via, F.Cu at (128.0, 54.0)
- added REF**: via, via:via, F.Cu at (129.0, 53.0)
- added REF**: via, via:via, F.Cu at (129.0, 84.0)
- added REF**: via, via:via, F.Cu at (128.0, 53.0)
- added REF**: via, via:via, F.Cu at (122.0, 48.0)
- added REF**: via, via:via, F.Cu at (121.0, 48.0)
- added REF**: via, via:via, F.Cu at (120.0, 48.0)
- added REF**: via, via:via, F.Cu at (119.0, 48.0)
- added REF**: via, via:via, F.Cu at (118.0, 48.0)
- added REF**: via, via:via, F.Cu at (117.0, 48.0)
- added REF**: via, via:via, F.Cu at (116.0, 48.0)
- added REF**: via, via:via, F.Cu at (115.0, 48.0)
- added REF**: via, via:via, F.Cu at (114.0, 48.0)
- added REF**: via, via:via, F.Cu at (128.0, 84.0)
- added REF**: via, via:via, F.Cu at (113.0, 48.0)
- added REF**: via, via:via, F.Cu at (112.0, 48.0)
- added REF**: via, via:via, F.Cu at (111.0, 48.0)
- added REF**: via, via:via, F.Cu at (110.0, 48.0)
- added REF**: via, via:via, F.Cu at (109.0, 48.0)
- added REF**: via, via:via, F.Cu at (108.0, 48.0)
- added REF**: via, via:via, F.Cu at (107.0, 48.0)
- added REF**: via, via:via, F.Cu at (106.0, 48.0)
- added REF**: via, via:via, F.Cu at (105.0, 48.0)
- added REF**: via, via:via, F.Cu at (104.0, 48.0)
- added REF**: via, via:via, F.Cu at (129.0, 83.0)
- added REF**: via, via:via, F.Cu at (103.0, 48.0)
- added REF**: via, via:via, F.Cu at (102.0, 48.0)
- added REF**: via, via:via, F.Cu at (101.0, 48.0)
- added REF**: via, via:via, F.Cu at (100.0, 48.0)
- added REF**: via, via:via, F.Cu at (99.0, 48.0)
- added REF**: via, via:via, F.Cu at (98.0, 48.0)
- added REF**: via, via:via, F.Cu at (97.0, 48.0)
- added REF**: via, via:via, F.Cu at (96.0, 48.0)
- added REF**: via, via:via, F.Cu at (95.0, 48.0)
- added REF**: via, via:via, F.Cu at (94.0, 48.0)
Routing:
- net GND: track 171.6 -> 108.2 mm, vias 65 -> 55
